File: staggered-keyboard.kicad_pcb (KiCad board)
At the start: 2 copper layers, 129 parts, among them U1 ProMicro

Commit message: Move diode in place
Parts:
- moved D63 330.3 mm to (335.0, 219.1)
- moved D64 324.0 mm to (358.0, 219.9)
- moved D28 319.3 mm to (357.2, 170.7)
- moved D54 308.7 mm to (342.9, 200.0)
- moved D41 300.9 mm to (335.0, 182.6)
- moved D27 297.9 mm to (331.8, 161.9)
- moved D14 286.4 mm to (350.0, 143.7)
- moved D62 282.1 mm to (311.9, 218.3)
- moved D26 270.8 mm to (312.7, 163.5)
- moved D53 270.6 mm to (305.6, 201.6)
- moved D13 268.2 mm to (321.5, 143.7)
- moved D40 267.7 mm to (315.9, 182.6)
- moved D52 263.9 mm to (288.1, 200.8)
- moved D24 254.6 mm to (274.6, 163.5)
- moved D11 248.7 mm to (282.6, 144.1)
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
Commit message: Update footprint for 1U switches & align diode for first row
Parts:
- D1, D10, D11, D12, D13, D14, D2, D3, D4, D5, D6, D7, D8, D9, U1: moved to B.Cu
- MX1, MX10, MX11, MX12, MX13, MX16, MX17, MX18, MX19, MX2, MX20, MX21, MX22, MX23, MX24, MX25, MX26, MX27, MX3, MX30, MX31, MX32, MX33, MX34, MX35, MX36, MX37, MX38, MX39, MX4, MX40, MX41, MX43, MX44, MX45, MX46, MX47, MX48, MX49, MX5, MX50, MX51, MX52, MX53, MX6, MX7, MX8, MX9: footprint Button_Switch_Keyboard:SW_Cherry_MX_1.00u_PCB -> MX_Only:MXOnly-1U-NoLED
- MX14: footprint Button_Switch_Keyboard:SW_Cherry_MX_2.00u_PCB -> MX_Only:MXOnly-2U-NoLED
- MX15: footprint Button_Switch_Keyboard:SW_Cherry_MX_1.50u_PCB -> MX_Only:MXOnly-1.5U-NoLED
- MX28: footprint Button_Switch_Keyboard:SW_Cherry_MX_ISOEnter_PCB -> MX_Only:MXOnly-ISO-NoLED
- moved U1 111.9 mm to (76.2, 156.4), turned to -90 degrees
- moved D1 14.0 mm to (103.5, 151.8), turned to 90 degrees
- moved D5 14.0 mm to (179.6, 151.8), turned to 90 degrees
- moved D4 13.9 mm to (160.6, 151.9), turned to 90 degrees
- moved D11 13.7 mm to (293.9, 151.8), turned to 90 degrees
- moved D10 13.4 mm to (274.9, 151.8), turned to 90 degrees
- moved D13 13.3 mm to (331.9, 151.8), turned to 90 degrees
- moved D3 13.3 mm to (141.5, 151.8), turned to 90 degrees
- moved D2 13.3 mm to (122.4, 151.8), turned to 90 degrees
- moved D14 13.2 mm to (360.4, 151.8), turned to 90 degrees
- moved D12 13.0 mm to (312.9, 151.8), turned to 90 degrees
- moved D8 12.7 mm to (236.8, 151.8), turned to 90 degrees
- moved D7 12.4 mm to (217.7, 151.8), turned to 90 degrees
- moved D9 12.4 mm to (255.8, 151.8), turned to 90 degrees
- moved D6 12.3 mm to (198.6, 151.8), turned to 90 degrees
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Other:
- board outline added: 306.4 x 95.3 mm

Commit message: Finish placing componants & Finish routing switches
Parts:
- D15, D16, D17, D18, D19, D20, D21, D22, D23, D24, D25, D26, D27, D28, D29, D30, D31, D32, D33, D34, D35, D36, D37, D38, D39, D40, D41, D42, D43, D44, D45, D46, D47, D48, D49, D50, D51, D52, D53, D54, D55, D56, D57, D58, D59, D60, D61, D62, D63, D64: moved to B.Cu
- U1: moved to F.Cu
- moved D63 16.5 mm to (348.8, 228.1), turned to 90 degrees
- moved D62 16.5 mm to (325.1, 228.1), turned to 90 degrees
- moved D17 15.8 mm to (151.0, 170.8), turned to 90 degrees
- moved D30 15.2 mm to (136.8, 189.9), turned to 90 degrees
- moved D37 15.2 mm to (270.1, 189.8), turned to 90 degrees
- moved D21 15.0 mm to (227.2, 170.8), turned to 90 degrees
- moved D53 14.9 mm to (317.8, 208.8), turned to 90 degrees
- moved D22 14.9 mm to (246.2, 170.8), turned to 90 degrees
- moved D49 14.8 mm to (241.6, 209.0), turned to 90 degrees
- moved D58 14.5 mm to (172.5, 227.8), turned to 90 degrees
- moved D23 14.4 mm to (265.3, 170.8), turned to 90 degrees
- moved D39 14.4 mm to (308.1, 189.9), turned to 90 degrees
- moved D31 14.3 mm to (155.9, 189.9), turned to 90 degrees
- moved D25 14.2 mm to (303.5, 170.8), turned to 90 degrees
- moved D41 14.1 mm to (346.3, 189.9), turned to 90 degrees
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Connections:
- U1 pad 16: unconnected-(U1-Pad16) -> Row 4
- U1 pad 17: unconnected-(U1-Pad17) -> Row 3
- U1 pad 18: unconnected-(U1-Pad18) -> Row 2
- U1 pad 19: unconnected-(U1-Pad19) -> Row 1
- U1 pad 20: unconnected-(U1-Pad20) -> Row 0
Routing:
- net Row 4: track 0.00 -> 342.8 mm
- net Row 3: track 0.00 -> 320.0 mm
- net Row 2: track 0.00 -> 295.9 mm
- net Row 1: track 0.00 -> 289.4 mm
- net Row 0: track 0.00 -> 268.7 mm
- net Col 11: track 0.00 -> 89.1 mm
- net Col 5: track 0.00 -> 88.9 mm
- net Col 3: track 0.00 -> 88.9 mm
- net Col 1: track 0.00 -> 87.2 mm
- net Col 10: track 0.00 -> 87.1 mm
- net Col 2: track 0.00 -> 87.1 mm
- net Col 8: track 0.00 -> 87.1 mm
- net Col 12: track 0.00 -> 87.1 mm
- net Col 13: track 0.00 -> 83.0 mm
- net Col 0: track 0.00 -> 82.1 mm
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
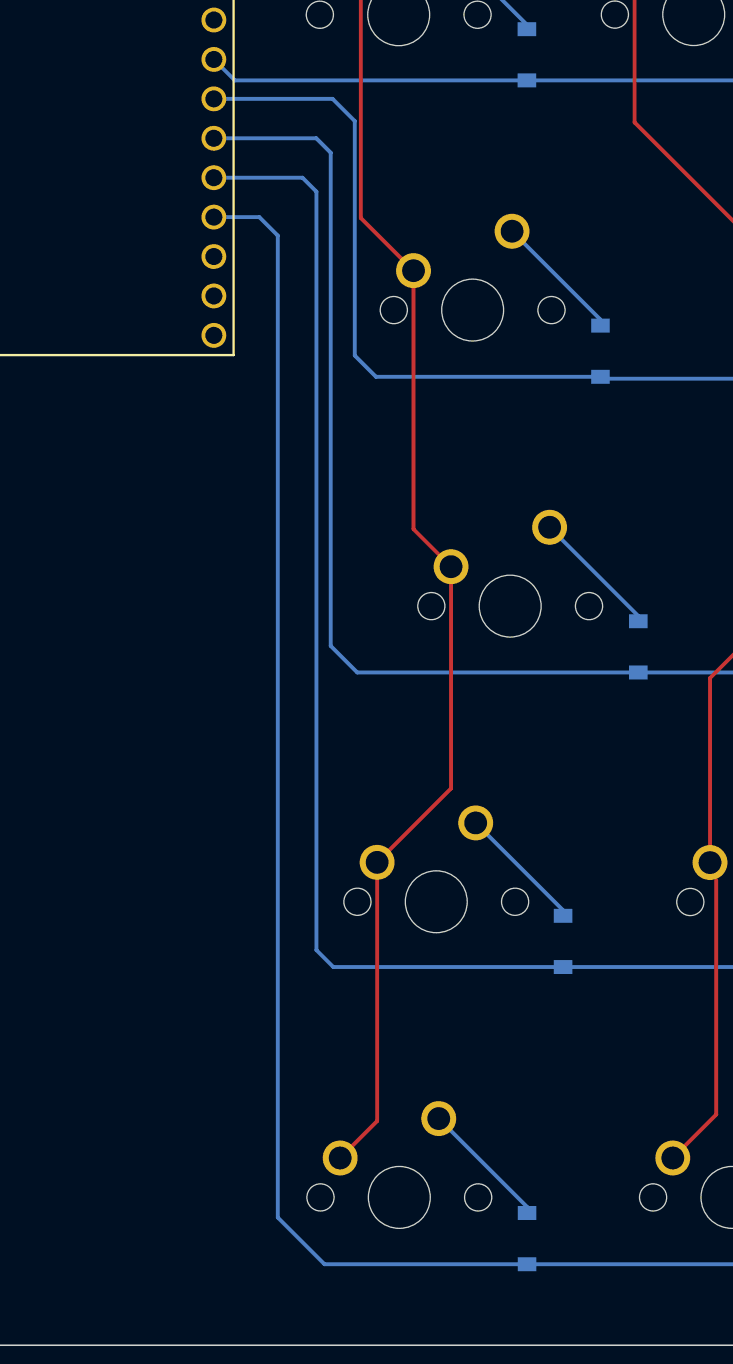
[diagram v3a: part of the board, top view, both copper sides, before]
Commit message: Clean up routing for rows
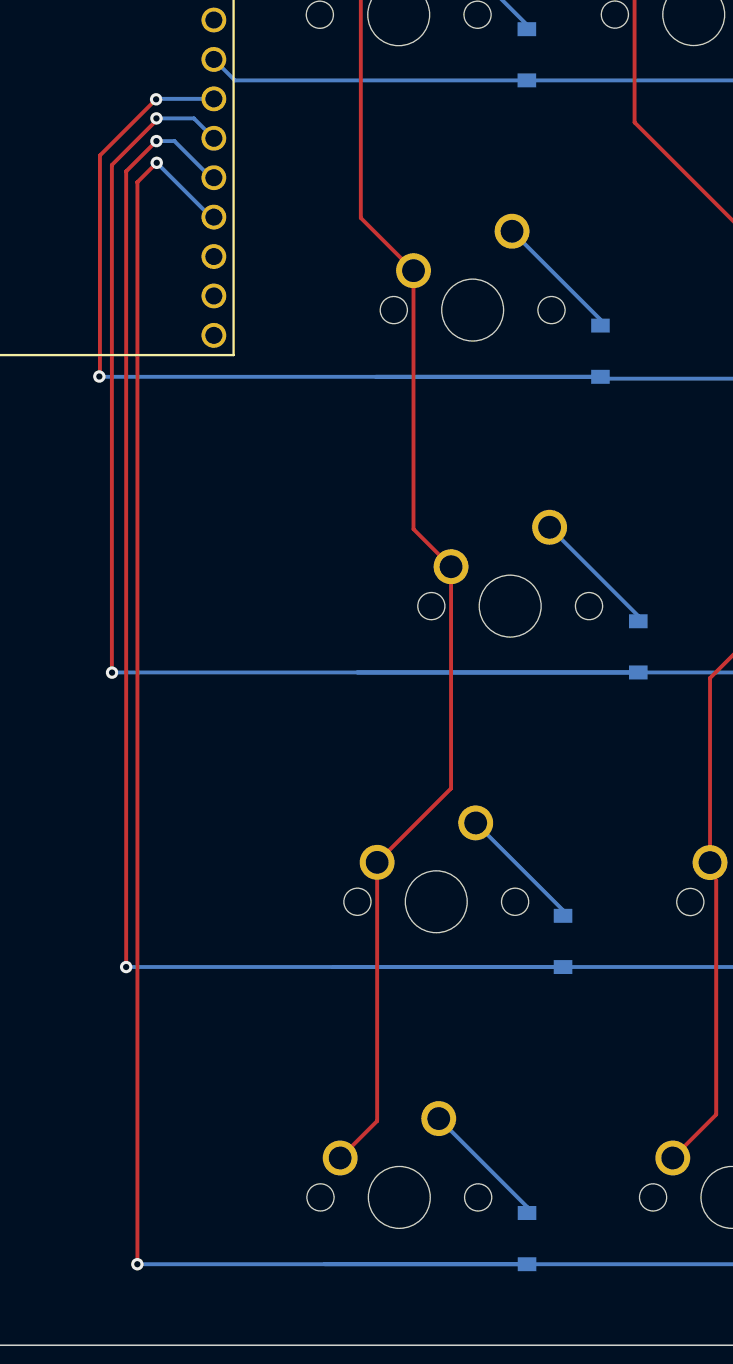
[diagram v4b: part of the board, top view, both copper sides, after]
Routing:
- net Row 2: track 295.9 -> 328.8 mm, vias 0 -> 2
- net Row 4: track 342.8 -> 372.4 mm, vias 0 -> 2
- net Row 3: track 320.0 -> 349.4 mm, vias 0 -> 2
- net Row 1: track 289.4 -> 318.1 mm, vias 0 -> 2
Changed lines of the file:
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@@
   (segment (start 354.82 153.49) (end 354.68 153.49) (width 0.25) (layer "B.Cu") (net 15))
   (segment (start 354.9025 144.1325) (end 354.9025 153.4075) (width 0.25) (layer "B.Cu") (net 15))
+  (segment (start 75.92 172.53) (end 75.96 172.49) (width 0.25) (layer "F.Cu") (net 16))
+  (segment (start 75.96 172.49) (end 75.96 158.29) (width 0.25) (layer "F.Cu") (net 16))
+  (segment (start 75.96 158.29) (end 79.58 154.67) (width 0.25) (layer "F.Cu") (net 16))
+  (via (at 79.58 154.67) (size 0.8) (drill 0.4) (layers "F.Cu" "B.Cu") (net 16))
+  (via (at 75.92 172.53) (size 0.8) (drill 0.4) (layers "F.Cu" "B.Cu") (net 16))
   (segment (start 108.33 172.67) (end 108.21 172.55) (width 0.25) (layer "B.Cu") (net 16))
-  (segment (start 92.38 171.18) (end 93.75 172.55) (width 0.25) (layer "B.Cu") (net 16))
+  (segment (start 75.94 172.55) (end 108.21 172.55) (width 0.25) (layer "B.Cu") (net 16))
+  (segment (start 79.61 154.64) (end 83.3 154.64) (width 0.25) (layer "B.Cu") (net 16))
   (segment (start 356.38 172.67) (end 108.33 172.67) (width 0.25) (layer "B.Cu") (net 16))
   (segment (start 93.75 172.55) (end 108.21 172.55) (width 0.25) (layer "B.Cu") (net 16))
-  (segment (start 90.95 154.64) (end 92.38 156.07) (width 0.25) (layer "B.Cu") (net 16))
-  (segment (start 92.38 156.07) (end 92.38 171.18) (width 0.25) (layer "B.Cu") (net 16))
-  (segment (start 83.3 154.64) (end 90.95 154.64) (width 0.25) (layer "B.Cu") (net 16))
+  (segment (start 75.92 172.53) (end 75.94 172.55) (width 0.25) (layer "B.Cu") (net 16))
+  (segment (start 79.58 154.67) (end 79.61 154.64) (width 0.25) (layer "B.Cu") (net 16))
   (segment (start 108.21 168.865) (end 108.21 169.25) (width 0.25) (layer "B.Cu") (net 17))
   (segment (start 102.515 163.17) (end 108.21 168.865) (width 0.25) (layer "B.Cu") (net 17))
@@
   (segment (start 359.7125 172.7025) (end 359.68 172.67) (width 0.25) (layer "B.Cu") (net 30))
   (segment (start 362.06125 172.7025) (end 359.7125 172.7025) (width 0.25) (layer "B.Cu") (net 30))
-  (segment (start 90.83 189.89) (end 92.54 191.6) (width 0.25) (layer "B.Cu") (net 31))
-  (segment (start 90.83 158.11) (end 90.83 189.89) (width 0.25) (layer "B.Cu") (net 31))
-  (segment (start 89.9 157.18) (end 90.83 158.11) (width 0.25) (layer "B.Cu") (net 31))
+  (segment (start 76.73 191.6) (end 76.74 191.61) (width 0.25) (layer "F.Cu") (net 31))
+  (segment (start 76.73 158.902868) (end 76.73 191.6) (width 0.25) (layer "F.Cu") (net 31))
+  (segment (start 79.6 156.032868) (end 76.73 158.902868) (width 0.25) (layer "F.Cu") (net 31))
+  (segment (start 79.6 155.9) (end 79.6 156.032868) (width 0.25) (layer "F.Cu") (net 31))
+  (via (at 76.74 191.61) (size 0.8) (drill 0.4) (layers "F.Cu" "B.Cu") (net 31))
+  (via (at 79.6 155.9) (size 0.8) (drill 0.4) (layers "F.Cu" "B.Cu") (net 31))
+  (segment (start 82.02 155.9) (end 83.3 157.18) (width 0.25) (layer "B.Cu") (net 31))
+  (segment (start 79.6 155.9) (end 82.02 155.9) (width 0.25) (layer "B.Cu") (net 31))
+  (segment (start 76.74 191.61) (end 76.75 191.6) (width 0.25) (layer "B.Cu") (net 31))
   (segment (start 92.54 191.6) (end 110.65 191.6) (width 0.25) (layer "B.Cu") (net 31))
-  (segment (start 83.3 157.18) (end 89.9 157.18) (width 0.25) (layer "B.Cu") (net 31))
+  (segment (start 76.75 191.6) (end 110.65 191.6) (width 0.25) (layer "B.Cu") (net 31))
   (segment (start 110.65 191.6) (end 346.25 191.6) (width 0.25) (layer "B.Cu") (net 31))
   (segment (start 346.25 191.6) (end 346.28 191.57) (width 0.25) (layer "B.Cu") (net 31))
@@
   (segment (start 346.28 187.8775) (end 346.28 188.27) (width 0.25) (layer "B.Cu") (net 44))
   (segment (start 340.63 182.2275) (end 346.28 187.8775) (width 0.25) (layer "B.Cu") (net 44))
+  (segment (start 77.65 159.31) (end 77.65 210.58) (width 0.25) (layer "F.Cu") (net 45))
+  (segment (start 79.6 157.36) (end 77.65 159.31) (width 0.25) (layer "F.Cu") (net 45))
+  (via (at 77.65 210.58) (size 0.8) (drill 0.4) (layers "F.Cu" "B.Cu") (net 45))
+  (via (at 79.6 157.36) (size 0.8) (drill 0.4) (layers "F.Cu" "B.Cu") (net 45))
+  (segment (start 80.76 157.36) (end 83.12 159.72) (width 0.25) (layer "B.Cu") (net 45))
   (segment (start 353.52 210.58) (end 353.56 210.54) (width 0.25) (layer "B.Cu") (net 45))
-  (segment (start 83.3 159.72) (end 89.01 159.72) (width 0.25) (layer "B.Cu") (net 45))
-  (segment (start 89.01 159.72) (end 89.91 160.62) (width 0.25) (layer "B.Cu") (net 45))
-  (segment (start 89.91 160.62) (end 89.91 209.49) (width 0.25) (layer "B.Cu") (net 45))
+  (segment (start 77.65 210.58) (end 105.8 210.58) (width 0.25) (layer "B.Cu") (net 45))
   (segment (start 91 210.58) (end 105.8 210.58) (width 0.25) (layer "B.Cu") (net 45))
+  (segment (start 79.6 157.36) (end 80.76 157.36) (width 0.25) (layer "B.Cu") (net 45))
   (segment (start 105.8 210.58) (end 353.52 210.58) (width 0.25) (layer "B.Cu") (net 45))
-  (segment (start 89.91 209.49) (end 91 210.58) (width 0.25) (layer "B.Cu") (net 45))
+  (segment (start 83.12 159.72) (end 83.3 159.72) (width 0.25) (layer "B.Cu") (net 45))
   (segment (start 100.17125 201.295) (end 105.8 206.92375) (width 0.25) (layer "B.Cu") (net 46))
   (segment (start 105.8 206.92375) (end 105.8 207.28) (width 0.25) (layer "B.Cu") (net 46))
@@
   (segment (start 353.56 207.03375) (end 353.56 207.24) (width 0.25) (layer "B.Cu") (net 58))
   (segment (start 347.82125 201.295) (end 353.56 207.03375) (width 0.25) (layer "B.Cu") (net 58))
+  (segment (start 78.375 160.015) (end 78.37 160.01) (width 0.25) (layer "F.Cu") (net 59))
+  (segment (start 78.37 229.73) (end 78.375 229.725) (width 0.25) (layer "F.Cu") (net 59))
+  (segment (start 78.37 160.01) (end 79.62 158.76) (width 0.25) (layer "F.Cu") (net 59))
+  (segment (start 78.375 229.725) (end 78.375 160.015) (width 0.25) (layer "F.Cu") (net 59))
+  (via (at 78.37 229.73) (size 0.8) (drill 0.4) (layers "F.Cu" "B.Cu") (net 59))
+  (via (at 79.62 158.76) (size 0.8) (drill 0.4) (layers "F.Cu" "B.Cu") (net 59))
+  (segment (start 79.62 158.76) (end 83.12 162.26) (width 0.25) (layer "B.Cu") (net 59))
   (segment (start 103.48 229.73) (end 361.07 229.73) (width 0.25) (layer "B.Cu") (net 59))
   (segment (start 361.07 229.73) (end 361.1 229.76) (width 0.25) (layer "B.Cu") (net 59))
-  (segment (start 87.42 226.72) (end 90.43 229.73) (width 0.25) (layer "B.Cu") (net 59))
-  (segment (start 83.3 162.26) (end 86.23 162.26) (width 0.25) (layer "B.Cu") (net 59))
-  (segment (start 87.42 163.45) (end 87.42 226.72) (width 0.25) (layer "B.Cu") (net 59))
   (segment (start 90.43 229.73) (end 103.48 229.73) (width 0.25) (layer "B.Cu") (net 59))
-  (segment (start 86.23 162.26) (end 87.42 163.45) (width 0.25) (layer "B.Cu") (net 59))
+  (segment (start 83.12 162.26) (end 83.3 162.26) (width 0.25) (layer "B.Cu") (net 59))
+  (segment (start 78.37 229.73) (end 103.48 229.73) (width 0.25) (layer "B.Cu") (net 59))
   (segment (start 103.48 226.035) (end 103.48 226.43) (width 0.25) (layer "B.Cu") (net 60))
   (segment (start 97.79 220.345) (end 103.48 226.035) (width 0.25) (layer "B.Cu") (net 60))

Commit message: Finish routing of the pcb & update layout in schematic
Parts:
- moved D64 14.2 mm to (362.8, 215.6)
- moved D28 6.53 mm to (363.7, 169.4), turned to 180 degrees
- moved D14 3.09 mm to (355.1, 155.9), turned to 90 degrees
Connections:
- D14 pad 1: Row 0 -> Row 4
- D28 pad 1: Row 1 -> Row 4
- MX14 pad 1: Col 13 -> Col 9
- MX28 pad 1: Col 13 -> Col 7
- MX64 pad 1: Col 13 -> Col 6
- U1 pad 1: unconnected-(U1-Pad1) -> Col 3
- U1 pad 10: unconnected-(U1-Pad10) -> Col 10
- U1 pad 11: unconnected-(U1-Pad11) -> Col 11
- U1 pad 12: unconnected-(U1-Pad12) -> Col 12
- U1 pad 13: unconnected-(U1-Pad13) -> Col 2
- U1 pad 14: unconnected-(U1-Pad14) -> Col 1
- U1 pad 15: unconnected-(U1-Pad15) -> Col 0
- U1 pad 2: unconnected-(U1-Pad2) -> Col 4
- U1 pad 5: unconnected-(U1-Pad5) -> Col 5
- U1 pad 6: unconnected-(U1-Pad6) -> Col 6
- U1 pad 7: unconnected-(U1-Pad7) -> Col 7
- U1 pad 8: unconnected-(U1-Pad8) -> Col 8
- U1 pad 9: unconnected-(U1-Pad9) -> Col 9
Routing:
- net Col 9: track 67.0 -> 409.2 mm, vias 0 -> 4
- net Col 6: track 67.0 -> 401.0 mm, vias 0 -> 3
- net Col 12: track 87.1 -> 403.9 mm, vias 0 -> 1
- net Col 7: track 67.0 -> 379.1 mm, vias 0 -> 2
- net Col 11: track 89.1 -> 372.9 mm, vias 0 -> 2
- net Col 10: track 87.1 -> 352.2 mm, vias 0 -> 2
- net Col 8: track 87.1 -> 283.3 mm, vias 0 -> 2
- net Col 5: track 88.9 -> 238.6 mm, vias 0 -> 2
- net Col 4: track 67.2 -> 174.5 mm
- net Col 3: track 88.9 -> 171.9 mm
- net Col 13: track 83.0 -> 0.00 mm
- net Row 4: track 372.4 -> 436.4 mm, vias 2 -> 1
- net Col 2: track 87.1 -> 140.4 mm, vias 0 -> 1
- net Col 1: track 87.2 -> 120.5 mm, vias 0 -> 1
- net Row 1: track 318.1 -> 295.9 mm, vias 2 -> 1
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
